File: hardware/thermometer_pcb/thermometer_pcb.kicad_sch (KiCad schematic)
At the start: 5 parts, among them IC1 STM32C071RBT6, U1 SHT4x

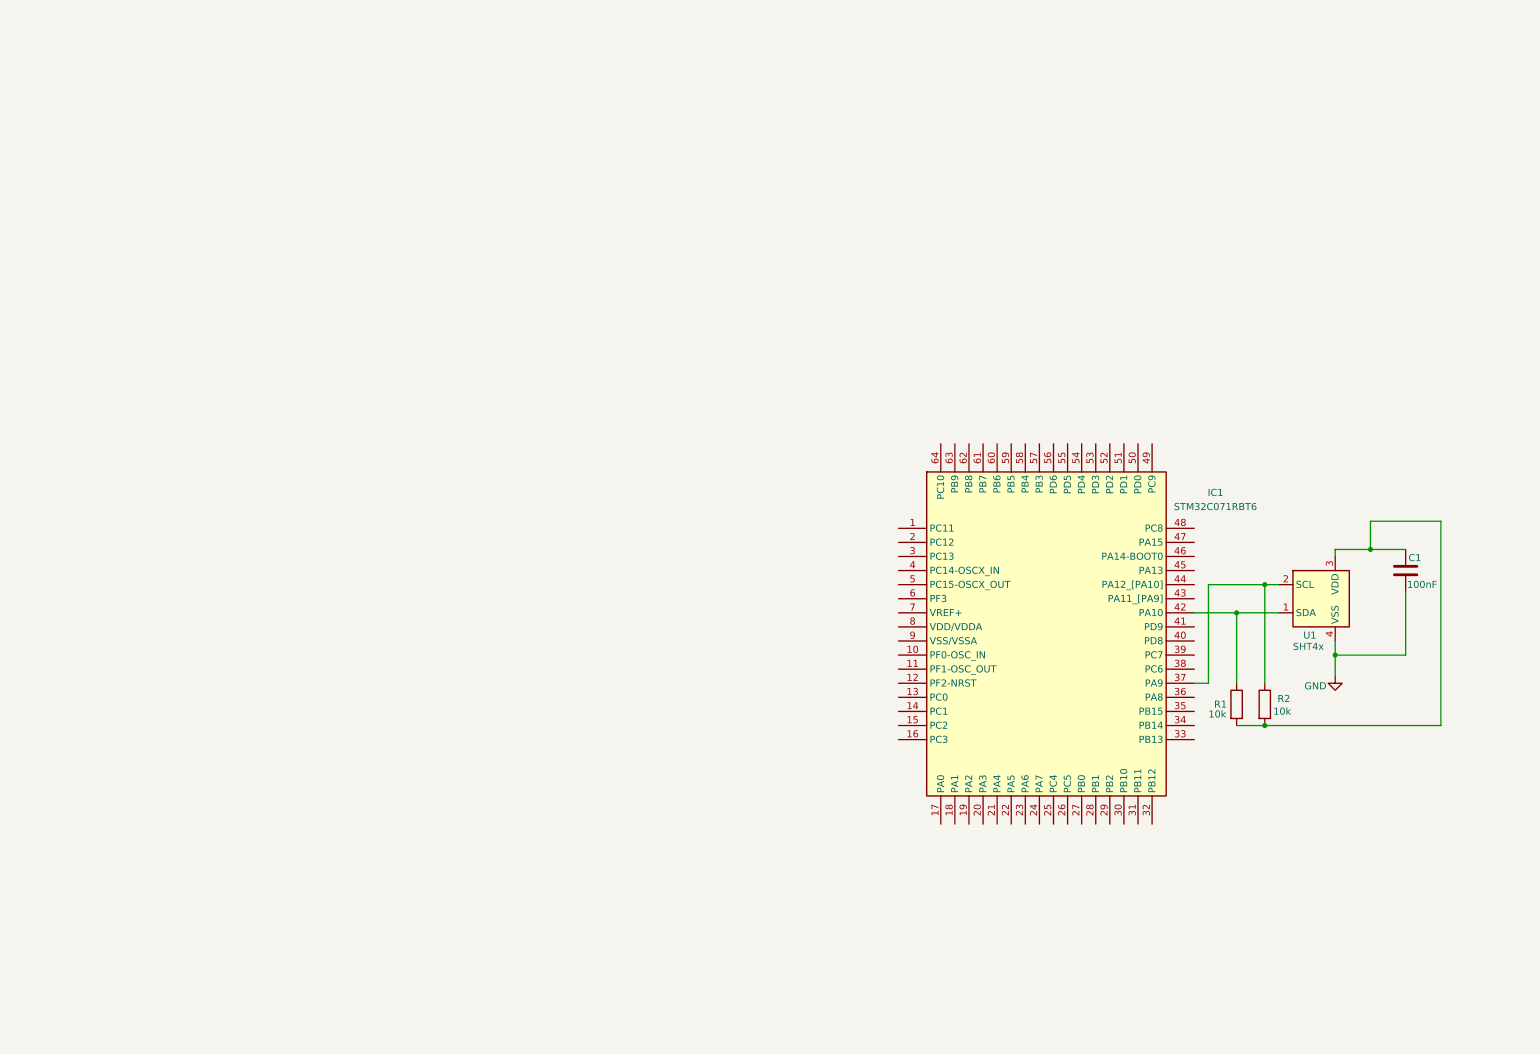
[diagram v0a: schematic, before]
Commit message: Added USB-C, 1x05 pin connector for SWD, refactoring
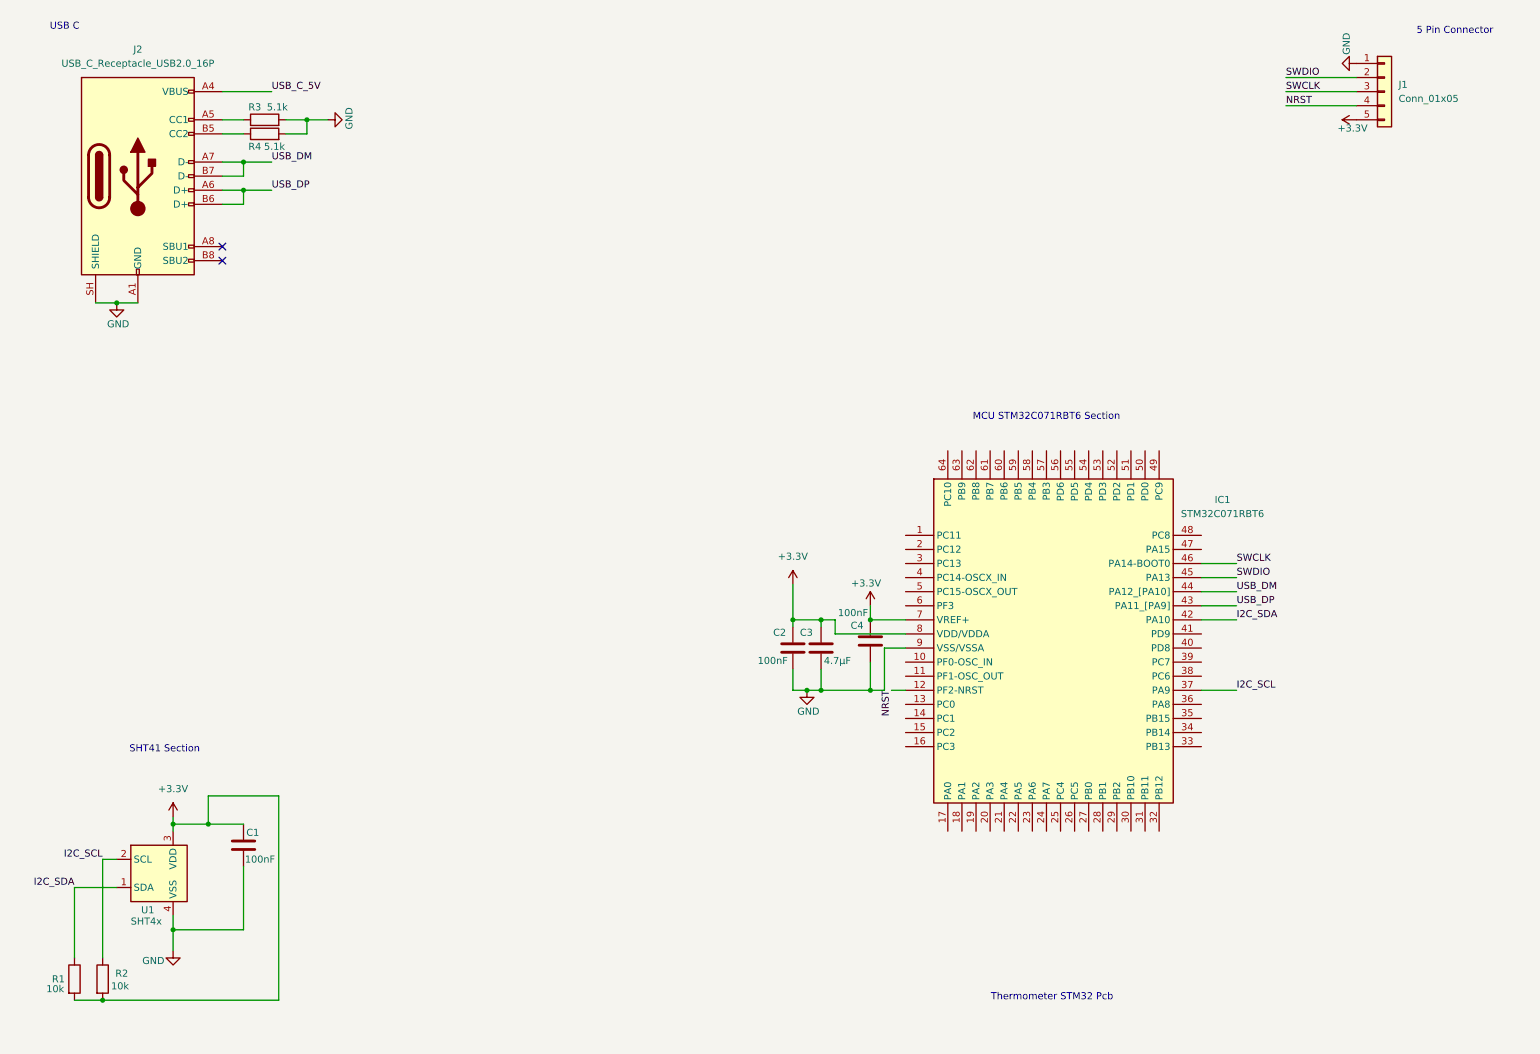
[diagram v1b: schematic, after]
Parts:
- added C2, C4: 100nF, symbol Device:C
- added C3: 4.7µF, symbol Device:C
- added J1: Conn_01x05, symbol Connector_Generic:Conn_01x05
- added J2: USB_C_Receptacle_USB2.0_16P, symbol Connector:USB_C_Receptacle_USB2.0_16P
- added R3, R4: 5.1k, Package_DIP:DIP-8_W7.62mm, symbol Device:R
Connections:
- net GND: now also IC1.9 (VSS/VSSA), C2.1, C3.1, C4.1, J1.1 (Pin_1), J2.A1 (GND), J2.A12 (GND), J2.B1 (GND), J2.B12 (GND), J2.SH (SHIELD), R3.2, R4.2
- net I2C_SDA: now reaches IC1.42 (PA10), R1.1, U1.1 (SDA)
- net I2C_SCL: now reaches IC1.37 (PA9), R2.1, U1.2 (SCL)
- net +3.3V: now reaches C1.2, R1.2, R2.2, U1.3 (VDD)
- net +3.3V: now also IC1.7 (VREF+), IC1.8 (VDD/VDDA), C2.2, C3.2, C4.2, J1.5 (Pin_5)
- net NRST: now reaches IC1.12 (PF2-NRST)
- net NRST: now also J1.4 (Pin_4)
- net USB_DP: now reaches IC1.43 (PA11_[PA9])
- net USB_DP: now also J2.A6 (D+), J2.B6 (D+)
- net USB_DM: now reaches IC1.44 (PA12_[PA10])
- net USB_DM: now also J2.A7 (D-), J2.B7 (D-)
- net SWDIO: now reaches IC1.45 (PA13)
- net SWDIO: now also J1.2 (Pin_2)
- net SWCLK: now reaches IC1.46 (PA14-BOOT0)
- net SWCLK: now also J1.3 (Pin_3)
- new net: J2.B5 (CC2), R4.1
- new net: J2.A5 (CC1), R3.1
- new net USB_C_5V: J2.A4 (VBUS), J2.A9 (VBUS), J2.B4 (VBUS), J2.B9 (VBUS)
- no-connect marks 0 -> 2
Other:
- note added: "5 Pin Connector"
- note added: "MCU STM32C071RBT6 Section"
- note added: "SHT41 Section"
- note added: "Thermometer STM32 Pcb"
- note added: "USB C"
- moved on the sheet: C1, IC1, R1, R2, U1

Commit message: started working on the charging circuit BQ24074RGTT
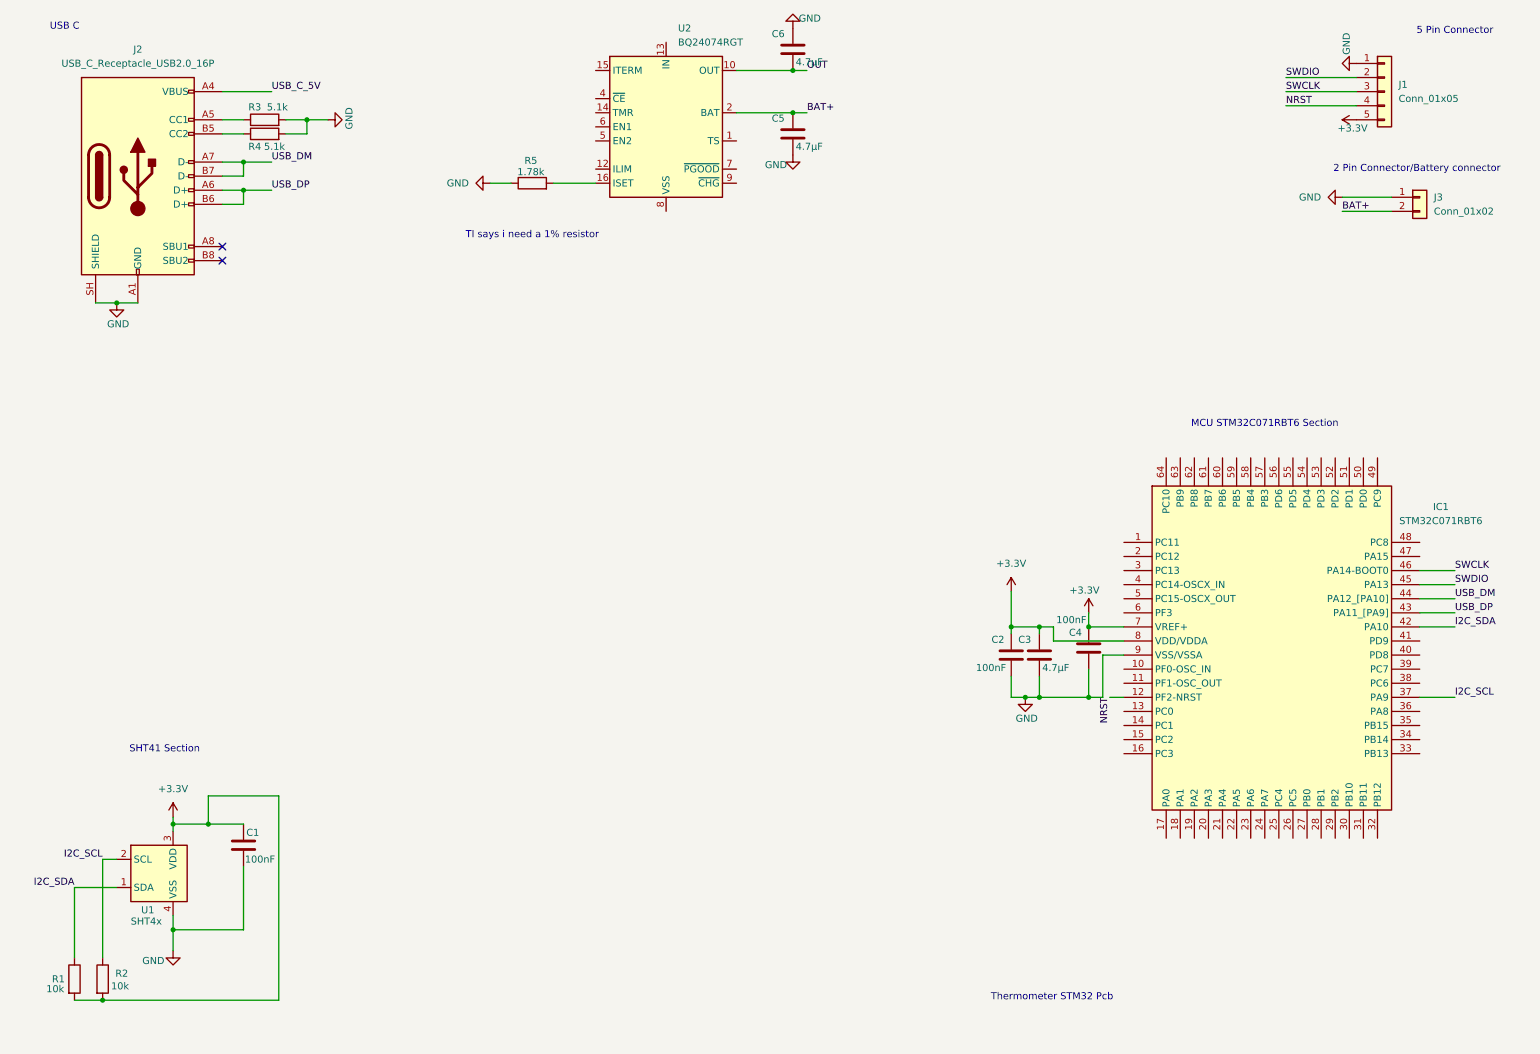
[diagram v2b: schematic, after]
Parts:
- added C5, C6: 4.7µF, symbol Device:C
- added J3: Conn_01x02, Connector_JST:JST_SH_SM02B-SRSS-TB_1x02-1MP_P1.00mm_Horizontal, symbol Connector_Generic:Conn_01x02
- added R5: 1.78k, symbol Device:R
- added U2: BQ24074RGT, Package_DFN_QFN:VQFN-16-1EP_3x3mm_P0.5mm_EP1.6x1.6mm, symbol Battery_Management:BQ24074RGT
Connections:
- net GND: now also C5.1, C6.2, J3.1 (Pin_1), R5.1
- new net: R5.2, U2.16 (ISET)
- new net: U2.17 (VSS), U2.8 (VSS)
- new net BAT+: C5.2, J3.2 (Pin_2), U2.2 (BAT), U2.3 (BAT)
- new net OUT: C6.1, U2.10 (OUT), U2.11 (OUT)
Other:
- note added: "2 Pin Connector/Battery connector"
- note added: "TI says i need a 1% resistor"
- moved on the sheet: C2, C3, C4, IC1

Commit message: finished implementing BQ24074.(for the first prototype)
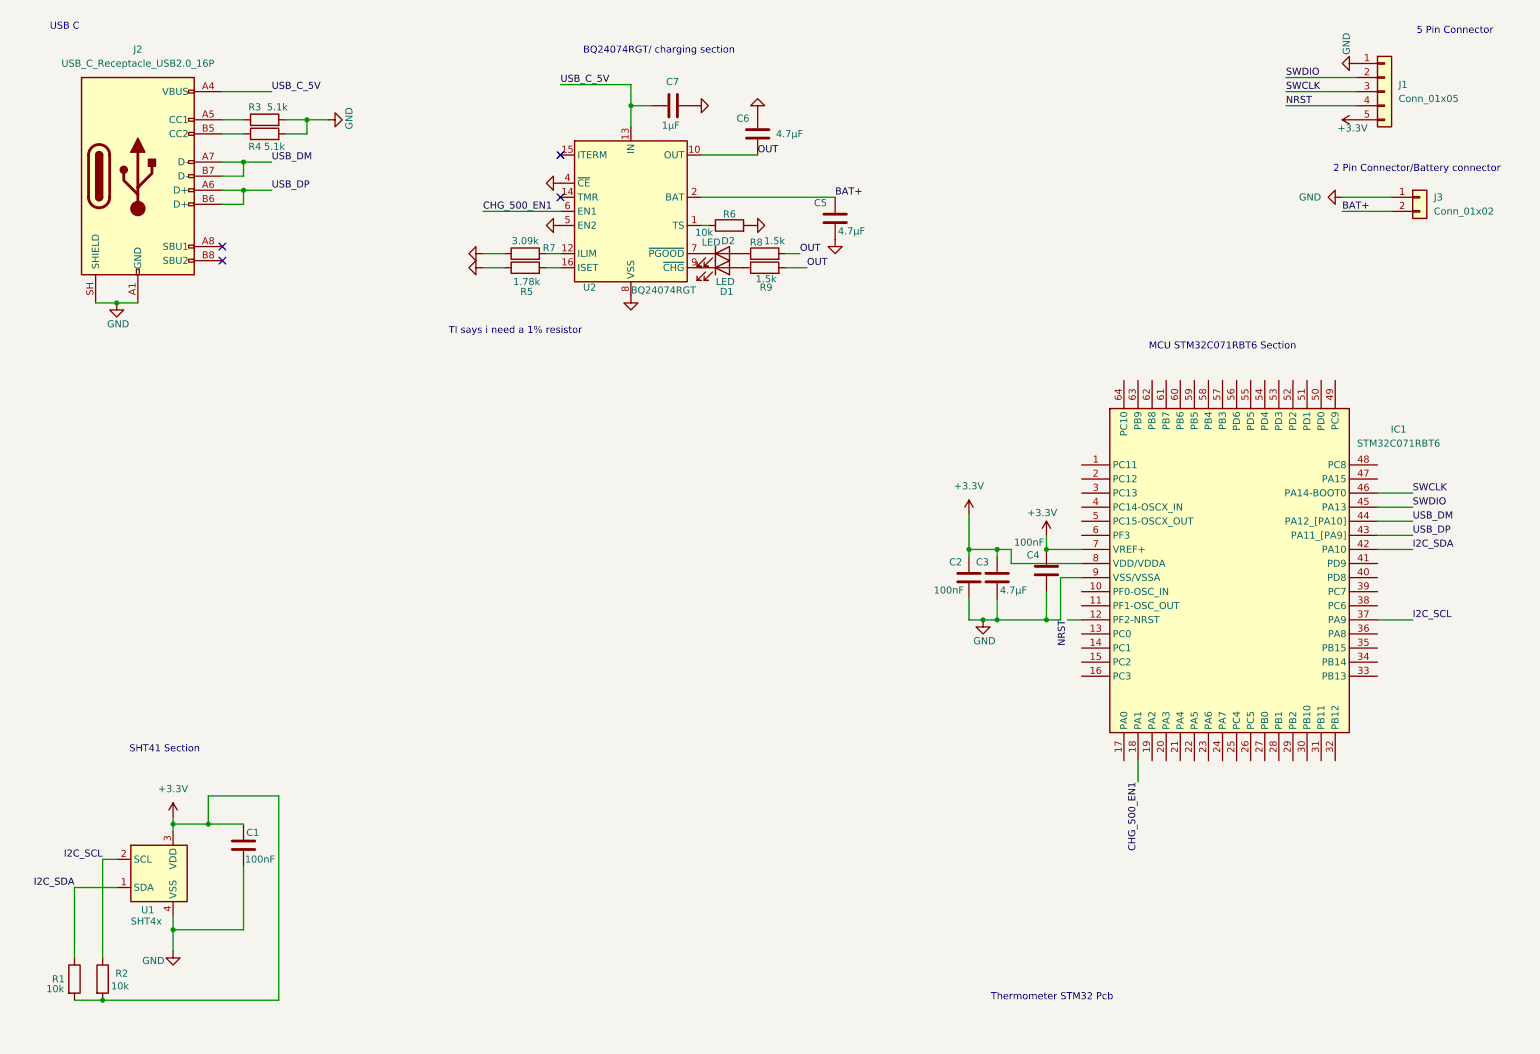
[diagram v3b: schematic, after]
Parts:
- added C7: 1µF, symbol Device:C
- added D1, D2: LED, symbol Device:LED
- added R6: 10k, symbol Device:R
- added R7: 3.09k, symbol Device:R
- added R8, R9: 1.5k, symbol Device:R
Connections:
- net GND: now also U2.17 (VSS), U2.4 (~{CE}), U2.5 (EN2), U2.8 (VSS), C7.2, R6.2, R7.1
- net OUT: now also R8.2, R9.2
- net USB_C_5V: now also U2.13 (IN), C7.1
- net CHG_500_EN1: now reaches IC1.18 (PA1)
- net CHG_500_EN1: now also U2.6 (EN1)
- net at U2.1 (TS): now also R6.1
- net at U2.12 (ILIM): now also R7.2
- net at U2.7 (~{PGOOD}): now also D2.1 (K)
- net at U2.9 (~{CHG}): now also D1.1 (K)
- new net: D2.2 (A), R8.1
- new net: D1.2 (A), R9.1
- no-connect marks 2 -> 4
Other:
- note added: "BQ24074RGT/ charging section"
- moved on the sheet: C2, C3, C4, C5, C6, IC1, R5, U2

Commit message: added voltage regulator for 3.3v
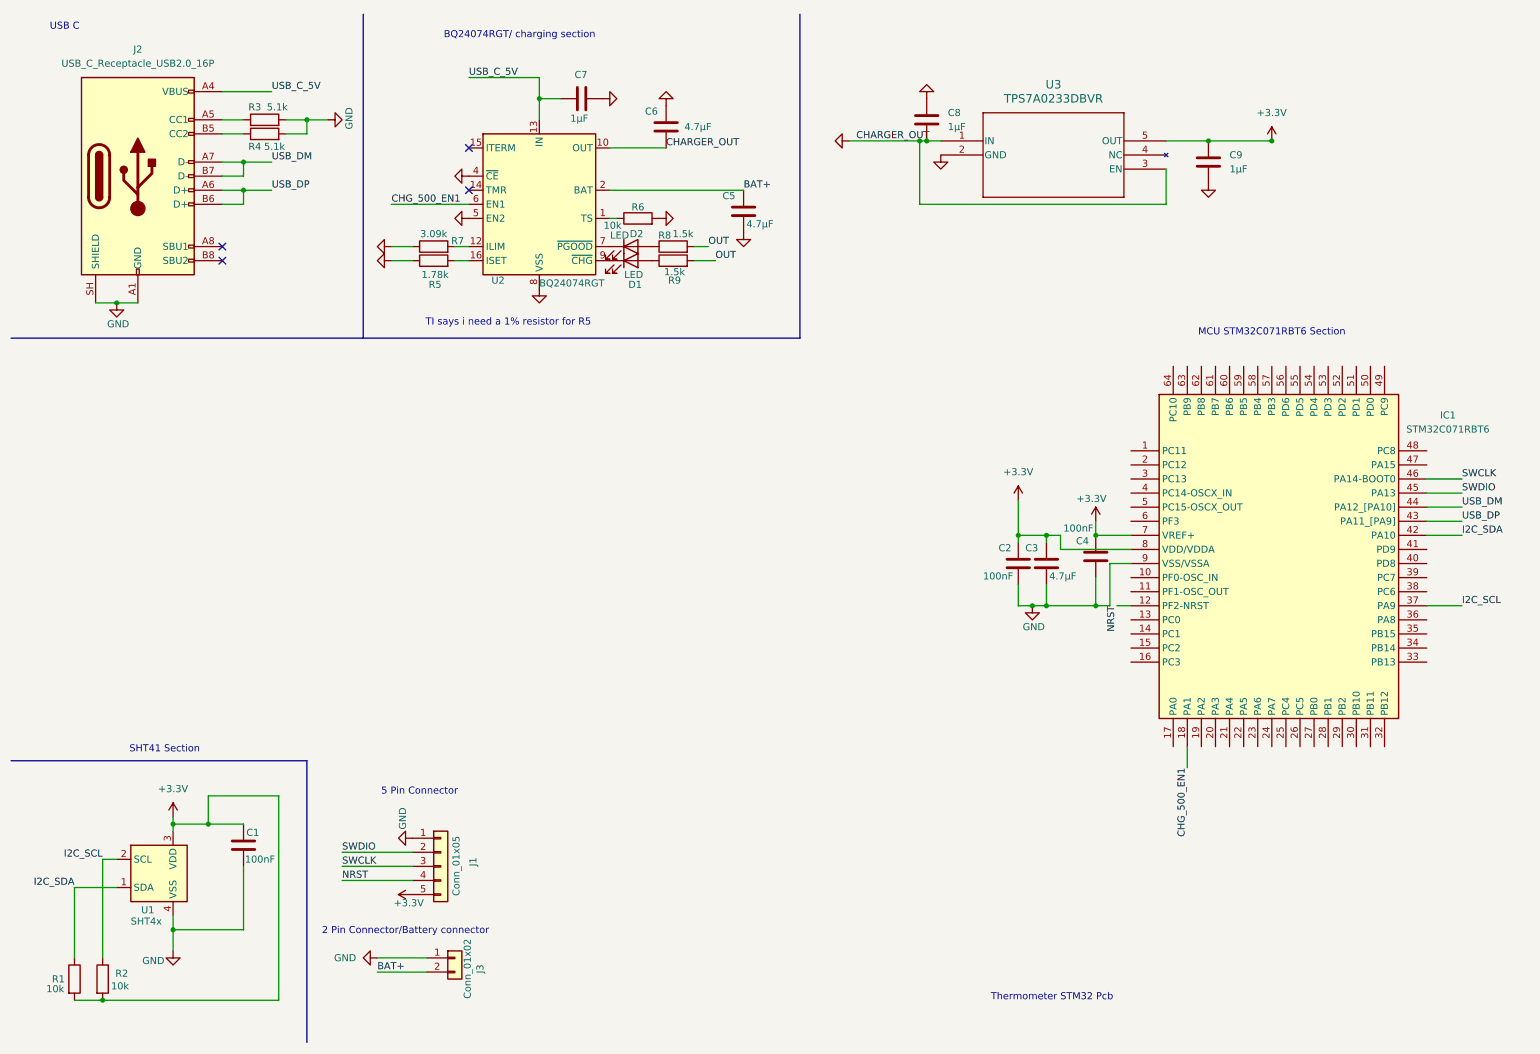
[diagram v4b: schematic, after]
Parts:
- added C8, C9: 1μF, symbol Device:C
- added U3: TPS7A0233DBVR, SOT23_DBV_TEX, symbol TPS7A0233DBVR:TPS7A0212PDBVR
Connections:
- net +3.3V: now also C9.1, U3.5 (OUT)
- net GND: now also C6.1, U2.10 (OUT), U2.11 (OUT), C8.1, C8.2, C9.2, U3.1 (IN), U3.2 (GND), U3.3 (EN)
- net OUT: no longer C6.1, U2.10 (OUT), U2.11 (OUT)
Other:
- note added: "TI says i need a 1% resistor for R5"
- note removed: "TI says i need a 1% resistor"
- moved on the sheet: C2, C3, C4, C5, C6, C7, D1, D2, IC1, J1, J3, R5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

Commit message: debbuged added footprints to components, added eink conn
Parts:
- added C10: 100nF, Capacitor_SMD:C_0805_2012Metric, symbol Device:C
- added C11: 4.7µF, Capacitor_SMD:C_0805_2012Metric, symbol Device:C
- added J4: Conn_01x08, Connector_JST:JST_PH_S8B-PH-K_1x08_P2.00mm_Horizontal, symbol Connector_Generic:Conn_01x08
- C1, C2, C3, C4, C5, C6, C7, C8, C9: footprint (none) -> Capacitor_SMD:C_0805_2012Metric
- D1, D2: footprint (none) -> LED_SMD:LED_0805_2012Metric
- J1: footprint (none) -> Connector_PinHeader_2.54mm:PinHeader_1x05_P2.54mm_Vertical
- J2: footprint (none) -> Connector_USB:USB_C_Receptacle_GCT_USB4105-xx-A_16P_TopMnt_Horizontal
- R1, R2, R3, R4: footprint Package_DIP:DIP-8_W7.62mm -> Resistor_SMD:R_0805_2012Metric
- R5: footprint (none) -> Resistor_SMD:R_0805_2012Metric; Tolerance (none) -> 1%
- R6, R7, R8, R9: footprint (none) -> Resistor_SMD:R_0805_2012Metric
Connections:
- net +3.3V: now also C10.1, C11.1, J4.1 (Pin_1)
- net GND: now also C10.2, C11.2, J4.2 (Pin_2); no longer C6.1, C8.2, U2.10 (OUT), U2.11 (OUT), U3.1 (IN), U3.3 (EN)
- net SPI_CS: now reaches IC1.21 (PA4)
- net SPI_CS: now also J4.5 (Pin_5)
- net SPI_CLK: now reaches IC1.22 (PA5)
- net SPI_CLK: now also J4.4 (Pin_4)
- net SPI_MOSI: now reaches IC1.24 (PA7)
- net SPI_MOSI: now also J4.3 (Pin_3)
- net EINK_DC: now reaches IC1.27 (PB0)
- net EINK_DC: now also J4.6 (Pin_6)
- net EINK_RST: now reaches IC1.28 (PB1)
- net EINK_RST: now also J4.7 (Pin_7)
- net EINK_BUSY: now reaches IC1.29 (PB2)
- net EINK_BUSY: now also J4.8 (Pin_8)
- net FRONT_LED: now reaches IC1.36 (PA8)
- net FRONT_LIGHT_BTN: now reaches IC1.38 (PC6)
- net OUT renamed CHARGER_OUT
- net CHARGER_OUT: now also C6.1, C8.2, U2.10 (OUT), U2.11 (OUT), U3.1 (IN), U3.3 (EN)
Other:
- note added: "3.3V Voltage Regulator"
- note added: "5 Pin Connector/SWD"
- note added: "8 Pin Eink Display Connector"
- note added: "Connectors"
- note added: "USB C 2.0"
- note removed: "5 Pin Connector"
- note removed: "USB C"
- moved on the sheet: C2, C3, C4, C8, C9, IC1, J1, J3, U3
